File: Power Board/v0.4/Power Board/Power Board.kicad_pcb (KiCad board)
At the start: 4 copper layers, 70 x 80 mm, 84 parts, among them J1 Battery In, J2 JST B2PS-VH, J3 JST B2PS-VH, J4 JST B2PS-VH, J5 JST B2PS-VH, J6 JST B2PS-VH, J7 JST B2PS-VH, J9 Raspberry Pi, Q1 SI5504BDC, SW1 SW_Push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

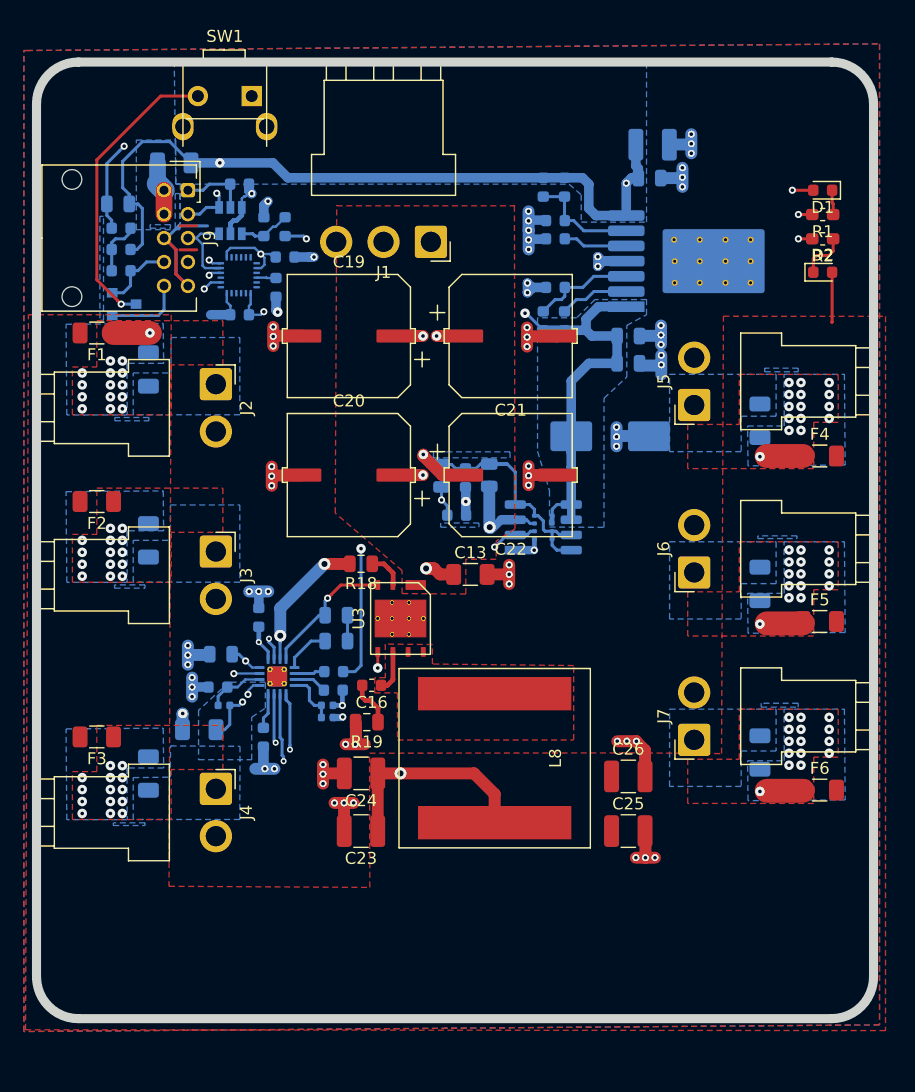
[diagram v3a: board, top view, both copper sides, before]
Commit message: Final Cleanup 2 DRC Errors that seem false Silkscreen needs work
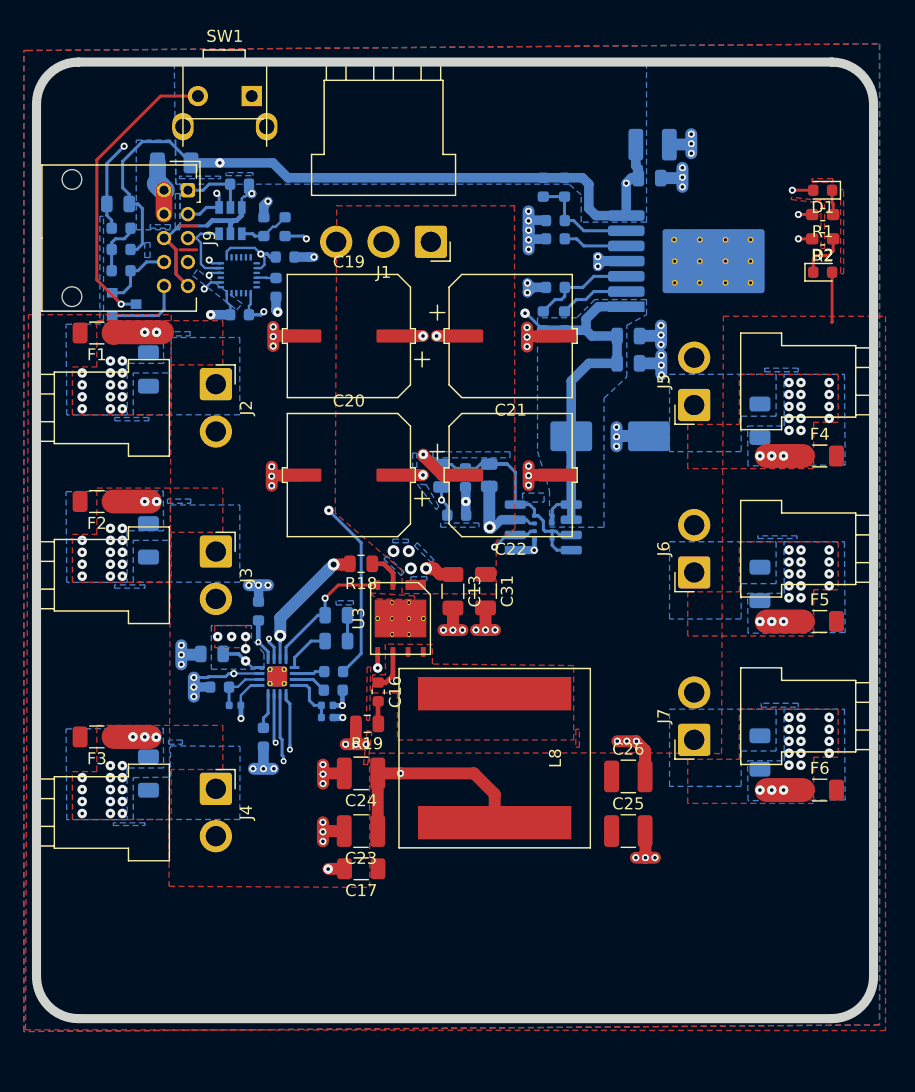
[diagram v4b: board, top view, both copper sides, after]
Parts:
- added C31: 10µF, Capacitor_SMD:C_1206_3216Metric, F.Cu at (114.5, 79.2)
- C17: moved to F.Cu
- moved C17 17.9 mm to (104.2, 102.5)
- moved C13 2.03 mm to (111.8, 79.3), turned to 270 degrees
- moved R20 0.93 mm to (93.6, 88.8)
- moved C16 0.78 mm to (105.6, 87.7), turned to 270 degrees
- moved C11 0.75 mm to (91.7, 84.5)
- moved C14 0.53 mm to (95.6, 80.9)
- moved R21 0.15 mm to (92.3, 87.3)
- moved R19 0.15 mm to (104.7, 90.3)
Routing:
- net GND: track 123.6 -> 132.8 mm, vias 74 -> 81
- net /Battery_Power: track 46.5 -> 53.0 mm, vias 8 -> 15
- net SDA: track 89.9 -> 93.1 mm
- net Net-(F3-Pad1): track 0.00 -> 3.04 mm, vias 14 -> 17
- net Net-(F2-Pad1): track 0.00 -> 3.04 mm, vias 14 -> 16
- net SCL: track 68.9 -> 71.3 mm
- net Net-(C16-Pad2): track 3.85 -> 1.75 mm
- net /Panel_Power: track 43.5 -> 42.0 mm, vias 3 -> 2
- net Net-(F1-Pad1): track 3.04 -> 4.02 mm, vias 15 -> 16
- net /5.2V_switched: track 136.5 -> 136.0 mm
- net Net-(F6-Pad1): vias 15 -> 17
- net Net-(F5-Pad1): vias 15 -> 17
- net Net-(F4-Pad1): vias 15 -> 17
- added copper zone on B.Cu, net /Battery_Power
- added copper zone on In2.Cu, net /Battery_Power
- removed copper zone on B.Cu, net /Panel_Power

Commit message: Rework routing to panel connectors.  WIP.
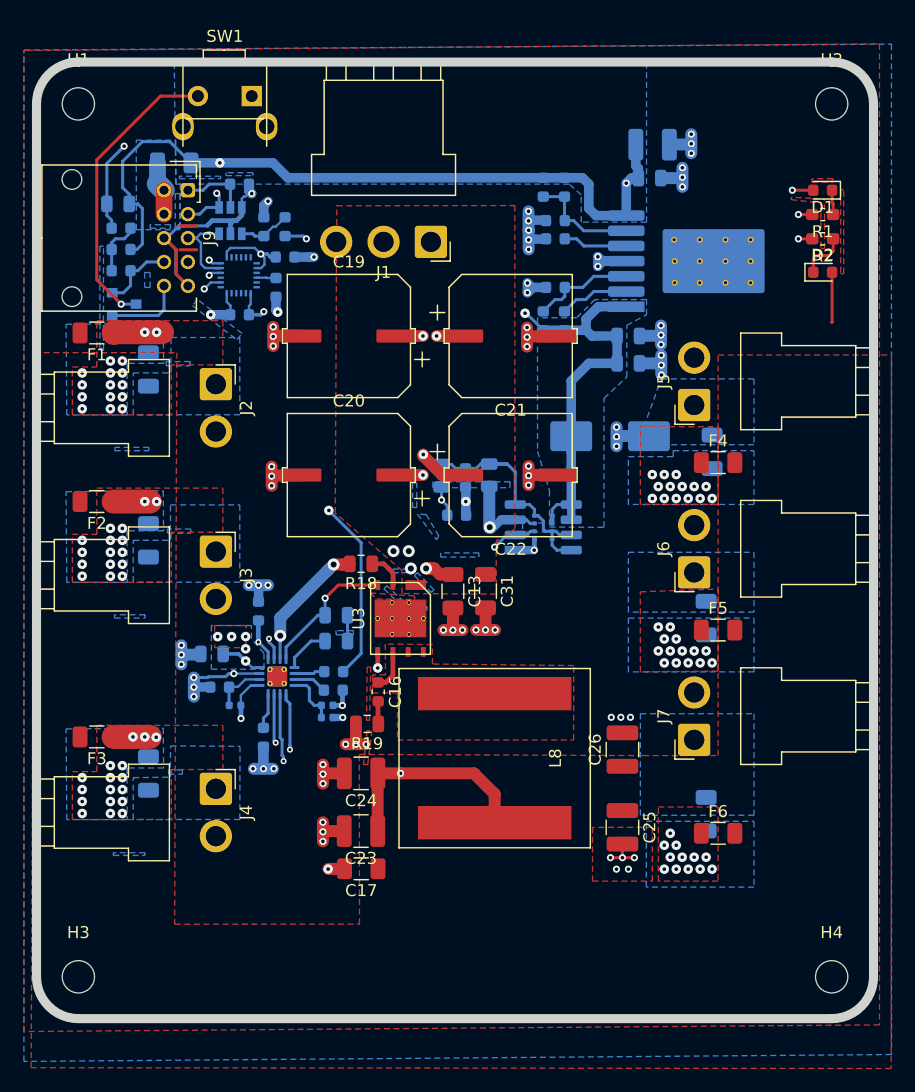
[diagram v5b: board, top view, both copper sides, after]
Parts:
- added H1: MountingHole, MountingHole:MountingHole_2.7mm_M2.5, F.Cu at (80.5, 38.5)
- added H2: MountingHole, MountingHole:MountingHole_2.7mm_M2.5, F.Cu at (143.5, 38.5)
- added H3: MountingHole, MountingHole:MountingHole_2.7mm_M2.5, F.Cu at (80.5, 111.5)
- added H4: MountingHole, MountingHole:MountingHole_2.7mm_M2.5, F.Cu at (143.5, 111.5)
- moved F6 9.24 mm to (134.0, 99.5)
- moved F5 8.53 mm to (134.0, 82.5)
- moved F4 8.52 mm to (134.0, 68.5)
- moved L6 6.85 mm to (133.0, 97.9)
- moved L5 5.33 mm to (133.0, 81.5)
- moved L4 4.77 mm to (133.5, 67.6)
- moved C26 2.30 mm to (126.0, 92.5), turned to 90 degrees
- moved C25 0.58 mm to (126.0, 99.0), turned to 270 degrees
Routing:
- net GND: track 132.8 -> 127.8 mm, vias 81 -> 83
- net Net-(F6-Pad1): track 3.04 -> 0.00 mm, vias 17 -> 12
- net Net-(F5-Pad1): track 3.04 -> 0.00 mm, vias 17 -> 14
- net Net-(F4-Pad1): track 3.04 -> 0.00 mm, vias 17 -> 14

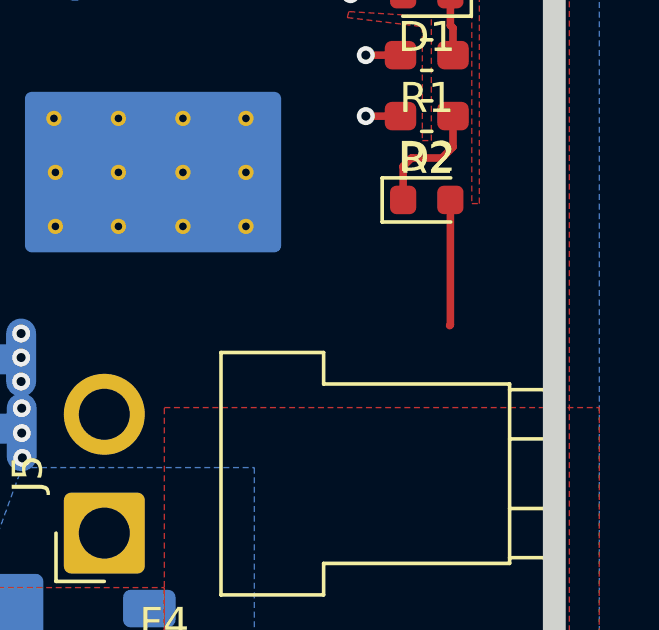
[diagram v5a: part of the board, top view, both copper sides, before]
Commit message: Reattach LED to Panel_Power.
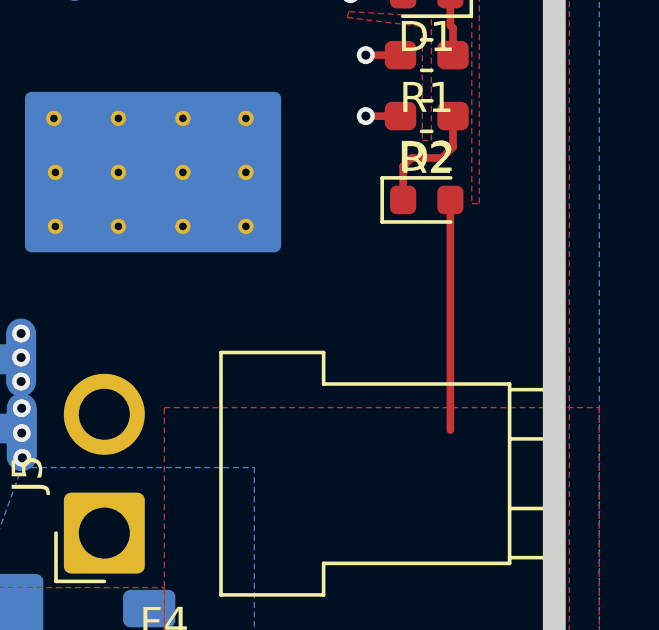
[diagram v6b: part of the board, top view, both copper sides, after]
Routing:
- net /Panel_Power: track 42.0 -> 45.4 mm
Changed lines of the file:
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@@
     (thickness 1.6)
     (drawings 17)
-    (tracks 755)
+    (tracks 754)
     (zones 0)
     (modules 89)
@@
   (page USLetter)
   (layers
-    (0 F.Cu signal hide)
+    (0 F.Cu signal)
     (1 In1.Cu signal hide)
     (2 In2.Cu signal hide)
@@
     (solder_mask_min_width 0.25)
     (aux_axis_origin 0 0)
-    (visible_elements FFFFF77F)
+    (visible_elements FFFFFF7F)
     (pcbplotparams
       (layerselection 0x010fc_ffffffff)
@@
   (segment (start 107.442 94.488) (end 105.54 94.488) (width 1) (layer F.Cu) (net 13))
   (via (at 107.442 94.488) (size 0.6) (drill 0.3) (layers F.Cu B.Cu) (net 13))
-  (segment (start 143.5355 56.7435) (end 143.51 56.769) (width 0.254) (layer F.Cu) (net 13))
-  (segment (start 143.5355 52.578) (end 143.5355 56.7435) (width 0.254) (layer F.Cu) (net 13))
   (via (at 94.100002 89.9) (size 0.6) (drill 0.3) (layers F.Cu B.Cu) (net 13))
   (segment (start 94.400001 90.199999) (end 94.100002 89.9) (width 0.254) (layer In2.Cu) (net 13))
@@
   (segment (start 104.45 90.75) (end 94.950002 90.75) (width 0.4) (layer In2.Cu) (net 13))
   (segment (start 107.442 94.488) (end 107.442 93.742) (width 0.4) (layer In2.Cu) (net 13))
+  (segment (start 143.5355 52.578) (end 143.5355 60.25) (width 0.254) (layer F.Cu) (net 13))
   (segment (start 143.623 47.752) (end 143.623 46.849) (width 0.254) (layer F.Cu) (net 14))
   (segment (start 143.5355 46.7615) (end 143.5355 45.72) (width 0.254) (layer F.Cu) (net 14))

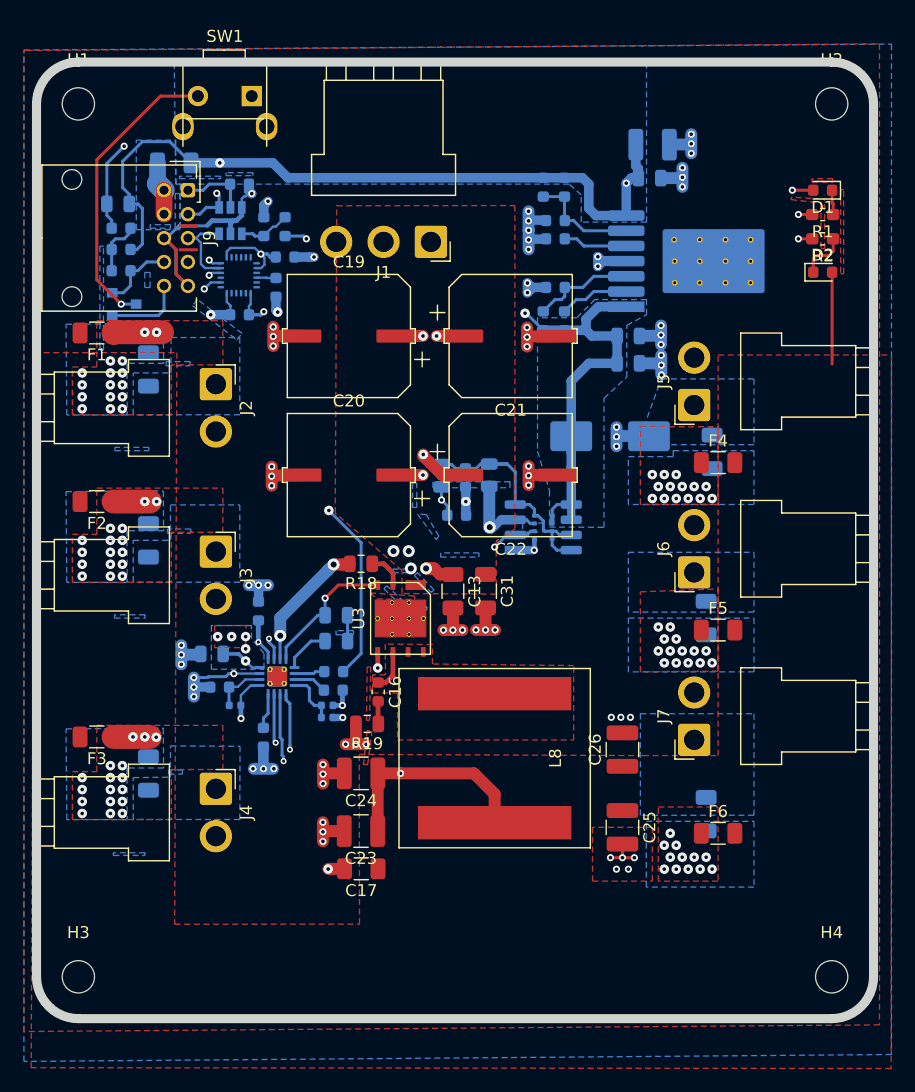
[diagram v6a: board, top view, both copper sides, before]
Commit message: Modified zones on the left side of the board
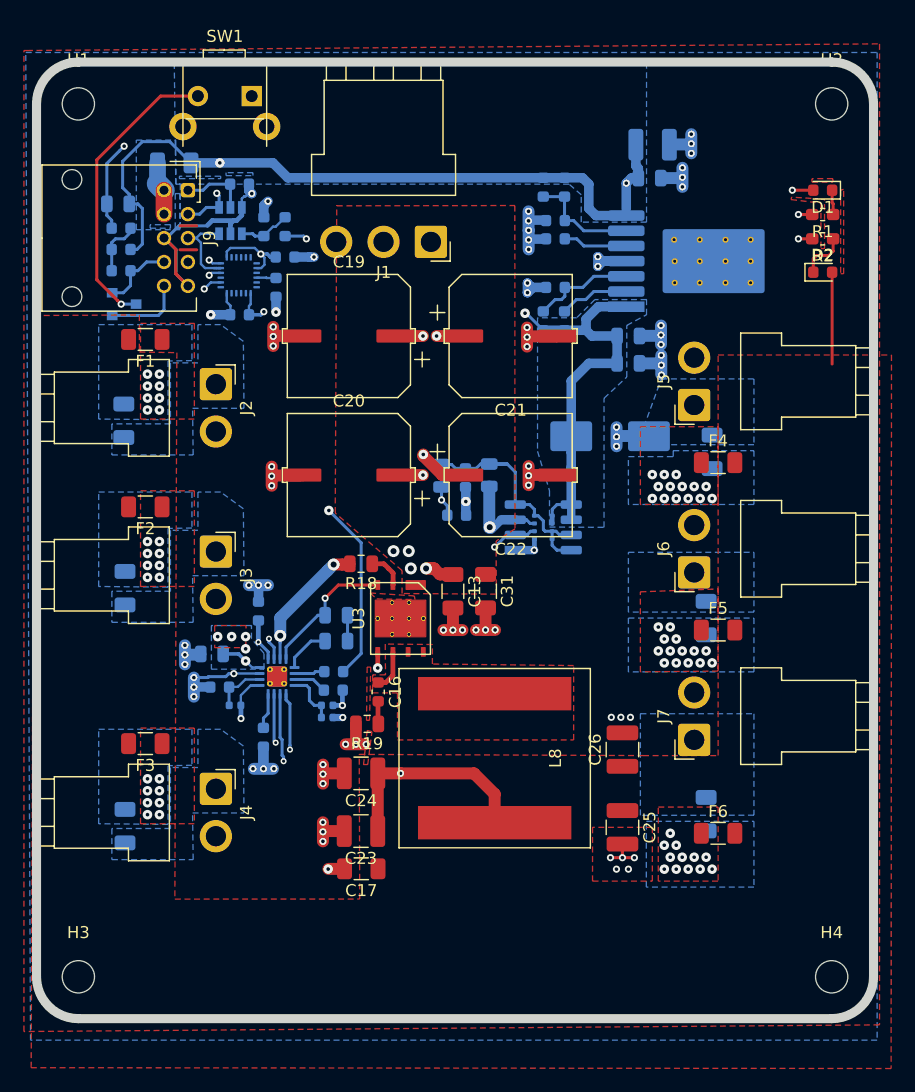
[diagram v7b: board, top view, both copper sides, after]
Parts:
- moved L3 4.82 mm to (84.4, 98.9)
- moved L1 4.76 mm to (84.3, 65.0)
- moved L2 4.45 mm to (84.4, 79.0)
- moved F3 4.10 mm to (86.1, 92.0)
- moved F1 4.09 mm to (86.1, 58.2)
- moved F2 4.08 mm to (86.1, 72.2)
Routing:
- net Net-(F1-Pad1): track 4.02 -> 0.00 mm, vias 16 -> 8
- net Net-(F3-Pad1): track 3.04 -> 0.00 mm, vias 17 -> 8
- net Net-(F2-Pad1): track 3.04 -> 0.00 mm, vias 16 -> 8

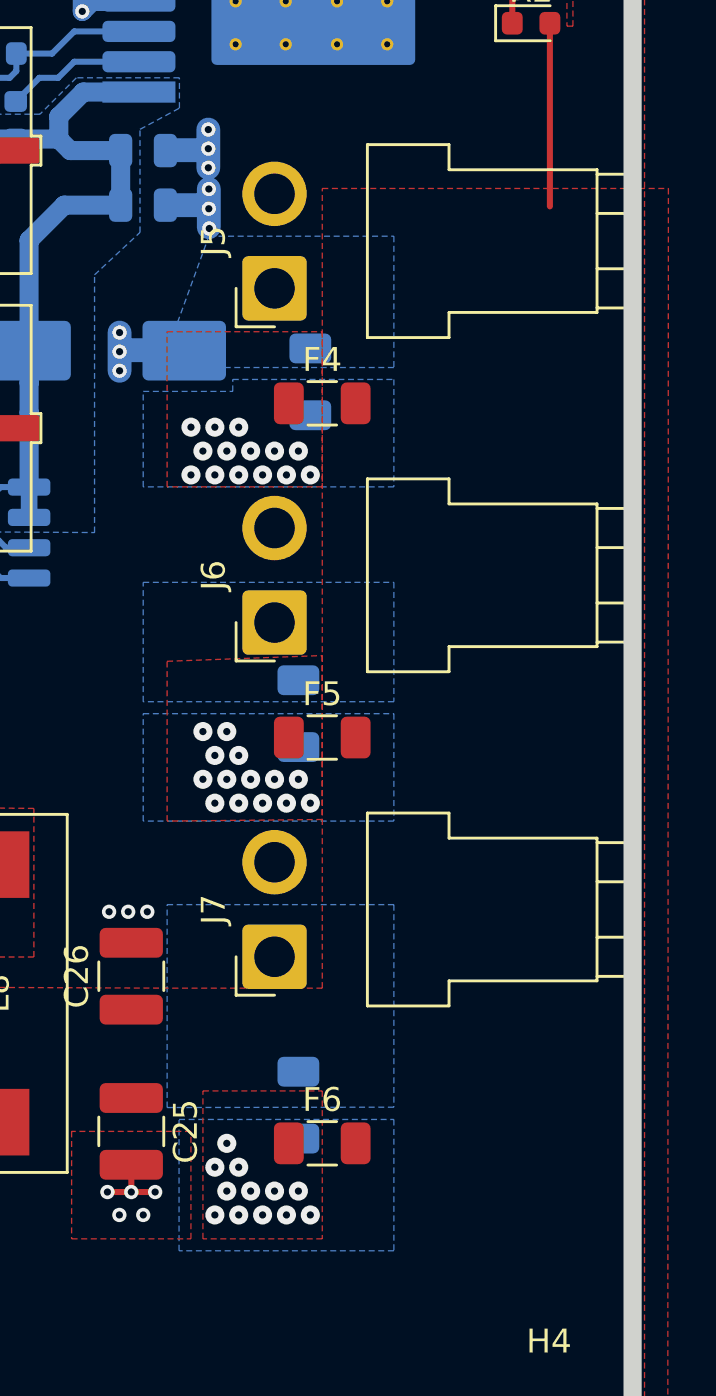
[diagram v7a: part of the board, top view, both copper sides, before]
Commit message: More Zones Changes/Improvements
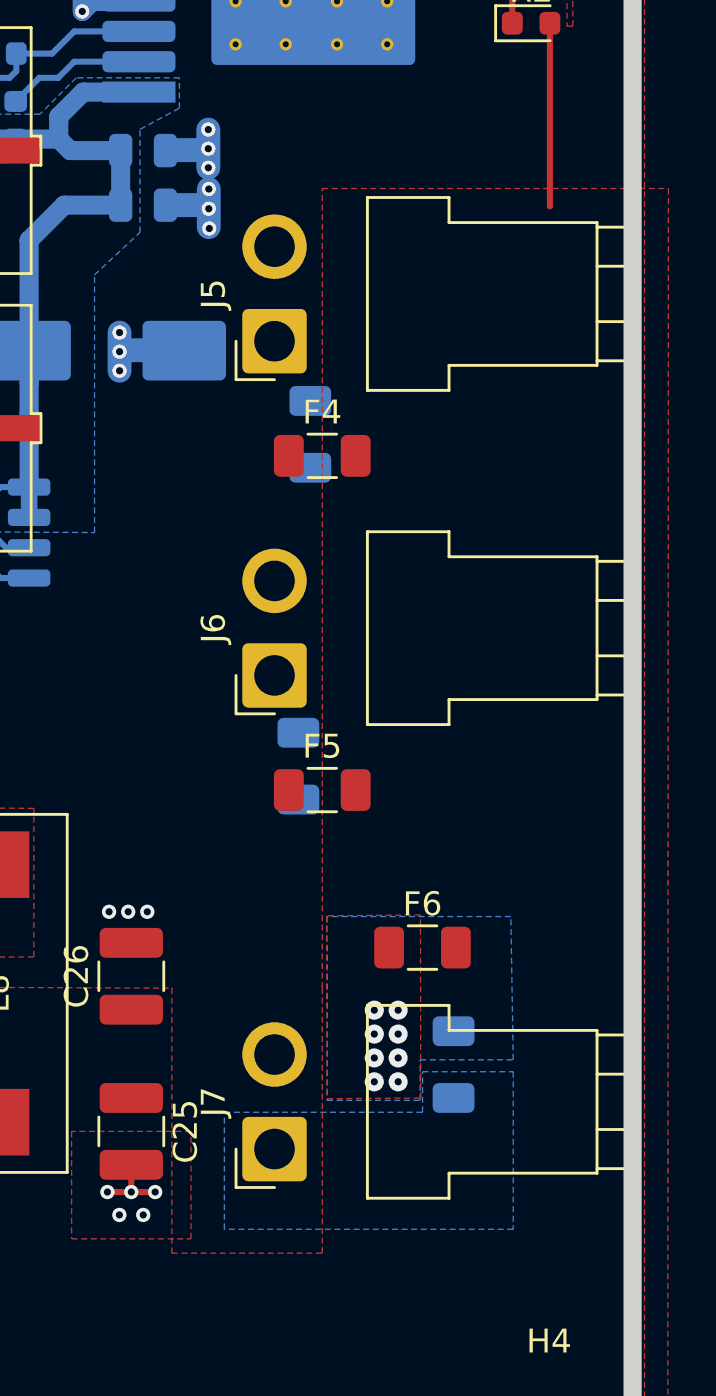
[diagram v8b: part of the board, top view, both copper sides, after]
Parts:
- moved F6 9.21 mm to (138.2, 91.3)
- moved J7 8.06 mm to (132.0, 99.7)
- moved L6 6.72 mm to (139.5, 96.2), turned to 270 degrees
- moved J5 2.21 mm to (132.0, 65.9)
- moved J6 2.21 mm to (132.0, 79.9)
- moved F4 2.20 mm to (134.0, 70.7)
- moved F5 2.20 mm to (134.0, 84.7)
- moved L4 2.20 mm to (133.5, 69.8)
- moved L5 2.20 mm to (133.0, 83.7)
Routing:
- net Net-(F6-Pad1): vias 12 -> 8
- net Net-(F5-Pad1): vias 14 -> 0
- net Net-(F4-Pad1): vias 14 -> 0
- removed copper zone on B.Cu, net Net-(F4-Pad1)
- removed copper zone on F.Cu, net Net-(F4-Pad1)
- removed copper zone on B.Cu, net Net-(F5-Pad1)
- removed copper zone on F.Cu, net Net-(F5-Pad1)
- removed copper zone on B.Cu, net Net-(J5-Pad1)
- removed copper zone on B.Cu, net Net-(J6-Pad1)
